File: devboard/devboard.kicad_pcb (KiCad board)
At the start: 4 copper layers, 60 x 95 mm, 147 parts, among them J1 Conn_01x02, J2 USB_C_Receptacle_USB2.0, J3 IN, J4 OUT, J5 Conn_01x02, J6 USB_C_Receptacle_USB2.0, J7 Conn_01x08, J8 Conn_01x03, Q1 DMN3300U, SW1 SW_Push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

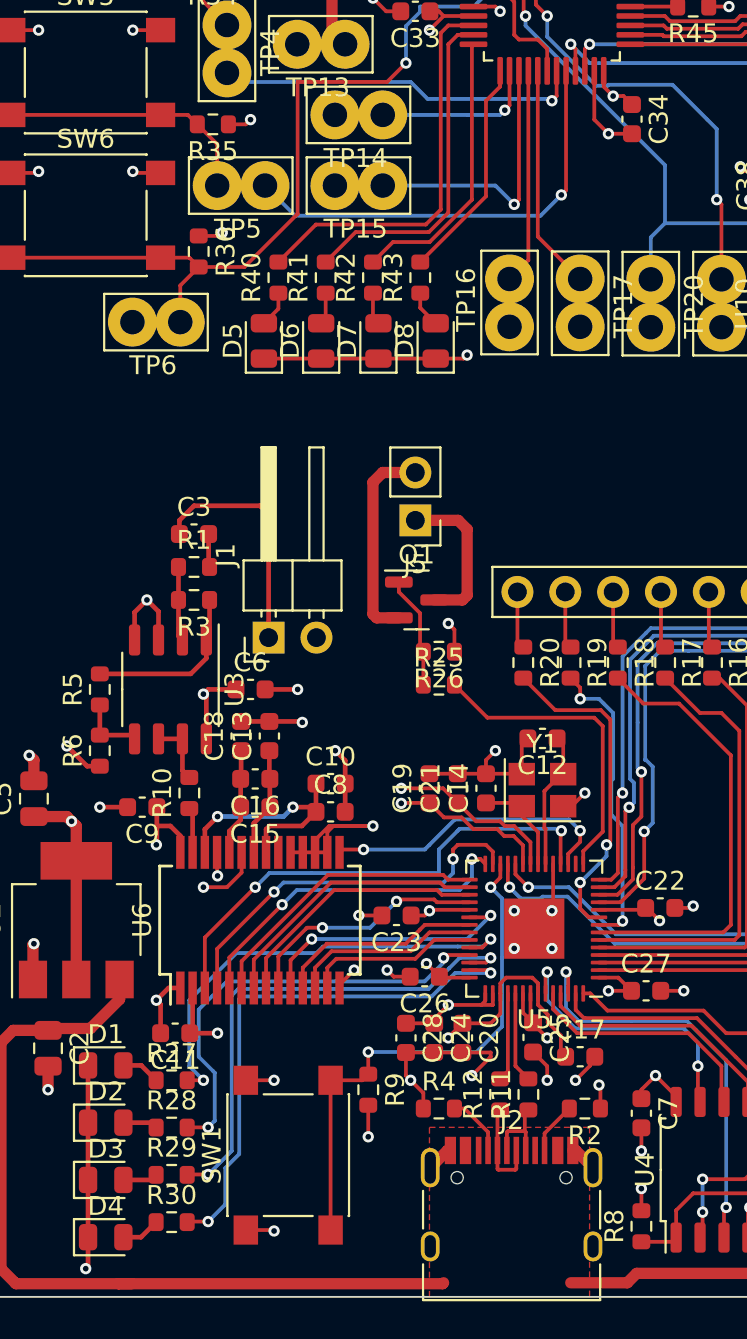
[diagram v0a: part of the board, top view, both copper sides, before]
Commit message: Small tweaks in hw design for proto order
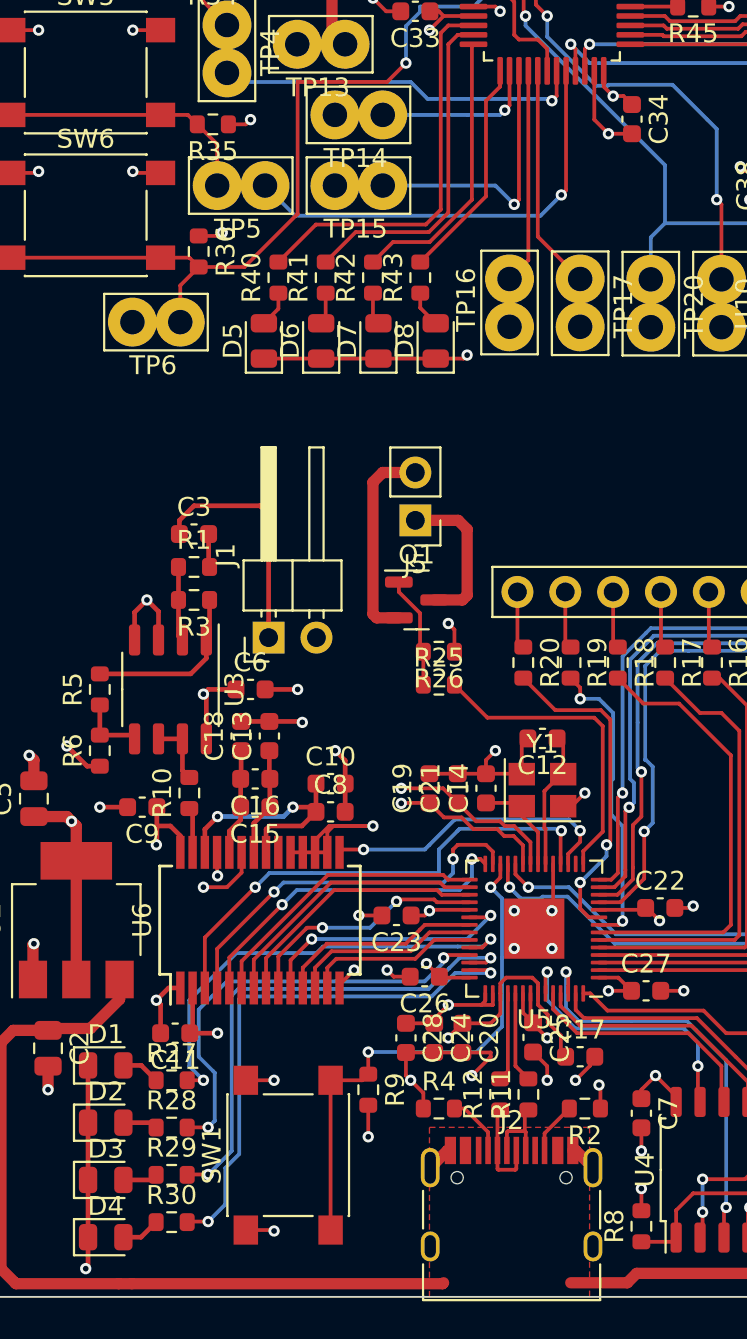
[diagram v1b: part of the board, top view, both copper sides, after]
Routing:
- net +5V: track 101.2 -> 100.5 mm
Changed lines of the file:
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@@
     (pad_to_mask_clearance 0)
     (pcbplotparams
-      (layerselection 0x00010fc_ffffffff)
+      (layerselection 0x003d0fc_ffffffff)
       (plot_on_all_layers_selection 0x0000000_00000000)
       (disableapertmacros false)
@@
       (drillshape 0)
       (scaleselection 1)
-      (outputdirectory "build")
+      (outputdirectory "gerbers")
     )
   )
@@
   (segment (start 156 149.25) (end 153 149.25) (width 0.6) (layer "F.Cu") (net 1))
   (segment (start 122.75 136.5) (end 122.75 148.5) (width 0.6) (layer "F.Cu") (net 1))
+  (segment (start 129.7 149.3) (end 146.2 149.3) (width 0.6) (layer "F.Cu") (net 1))
   (segment (start 153.2545 70.155) (end 153.0995 70) (width 0.2) (layer "F.Cu") (net 1))
   (segment (start 176.8 146.4) (end 176.8 148.2) (width 0.6) (layer "F.Cu") (net 1))
@@
   (segment (start 160.55 64.5) (end 160.55 62.6) (width 0.6) (layer "F.Cu") (net 1))
   (segment (start 179.25 146.75) (end 177.15 146.75) (width 0.6) (layer "F.Cu") (net 1))
-  (segment (start 129 149.3) (end 146.2 149.3) (width 0.6) (layer "F.Cu") (net 1))
   (segment (start 156.38 70.155) (end 156.475 70.25) (width 0.2) (layer "F.Cu") (net 1))
   (segment (start 161.1 62.05) (end 159.05 62.05) (width 0.6) (layer "F.Cu") (net 1))
-  (segment (start 146.2 149.3) (end 146.25 149.25) (width 0.6) (layer "F.Cu") (net 1))
   (segment (start 154.375 70.155) (end 153.2545 70.155) (width 0.2) (layer "F.Cu") (net 1))
   (segment (start 122.75 148.5) (end 123.5 149.25) (width 0.6) (layer "F.Cu") (net 1))
@@
   (segment (start 156.5 148.75) (end 156 149.25) (width 0.6) (layer "F.Cu") (net 1))
   (segment (start 129.05 134.2) (end 127.5 135.75) (width 0.6) (layer "F.Cu") (net 1))
+  (segment (start 146.2 149.3) (end 146.25 149.25) (width 0.6) (layer "F.Cu") (net 1))
   (segment (start 176.25 148.75) (end 156.5 148.75) (width 0.6) (layer "F.Cu") (net 1))
   (segment (start 149.37 63.3995) (end 149.4705 63.5) (width 0.6) (layer "F.Cu") (net 1))
@@
   (segment (start 123.275 90.33) (end 124.67 90.33) (width 0.2) (layer "F.Cu") (net 5))
   (segment (start 146.225 123) (end 144 123) (width 0.2) (layer "F.Cu") (net 5))
-  (segment (start 155 133.75) (end 156.225 133.75) (width 0.2) (layer "F.Cu") (net 5))
   (segment (start 147.625 133.05) (end 146.075 133.05) (width 0.2) (layer "F.Cu") (net 5))
   (segment (start 131.225 90.33) (end 129.83 90.33) (width 0.2) (layer "F.Cu") (net 5))
@@
   (segment (start 124.91 67.59) (end 125 67.5) (width 0.2) (layer "F.Cu") (net 5))
   (segment (start 150.8625 133.8875) (end 150.8625 135.3125) (width 0.2) (layer "F.Cu") (net 5))
+  (segment (start 155 133.75) (end 156.225 133.75) (width 0.2) (layer "F.Cu") (net 5))
   (segment (start 161.1 59.75) (end 167.4 59.75) (width 0.6) (layer "F.Cu") (net 5))
   (segment (start 150.8625 127.0125) (end 150.8625 125.8625) (width 0.2) (layer "F.Cu") (net 5))
-  (segment (start 156.225 133.75) (end 156.25 133.75) (width 0.2) (layer "F.Cu") (net 5))
   (segment (start 132.775 136) (end 134.25 136) (width 0.25) (layer "F.Cu") (net 5))
   (segment (start 156.75 145.425) (end 156.75 144.25) (width 0.2) (layer "F.Cu") (net 5))
@@
   (via (at 153.5 128) (size 0.6) (drill 0.3) (layers "F.Cu" "B.Cu") (net 74))
   (segment (start 153.5 128) (end 154.9005 126.5995) (width 0.2) (layer "B.Cu") (net 74))
-  (segment (start 154.75 126.1505) (end 154.9005 126) (width 0.2) (layer "B.Cu") (net 74))
   (segment (start 154.9005 126.5995) (end 154.9005 126) (width 0.2) (layer "B.Cu") (net 74))
   (segment (start 156.8995 127.797556) (end 156.8995 125.291143) (width 0.2) (layer "F.Cu") (net 75))
@@
   (segment (start 149.75 86.75) (end 149.75 84.9125) (width 0.2) (layer "F.Cu") (net 110))
   (via (at 149.5 87) (size 0.6) (drill 0.3) (layers "F.Cu" "B.Cu") (net 110))
-  (segment (start 147.5 87.25) (end 149.25 87.25) (width 0.2) (layer "B.Cu") (net 110))
+  (segment (start 147.75 87.25) (end 149.25 87.25) (width 0.2) (layer "B.Cu") (net 110))
   (segment (start 147.75 87.25) (end 147.5 87.25) (width 0.2) (layer "B.Cu") (net 110))
   (segment (start 147.5 87.25) (end 143.02 87.25) (width 0.2) (layer "B.Cu") (net 110))
